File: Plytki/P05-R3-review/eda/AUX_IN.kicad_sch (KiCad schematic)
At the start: 11 parts, among them J6 AUX / coax 50mm, SW1 AUX HI / LO

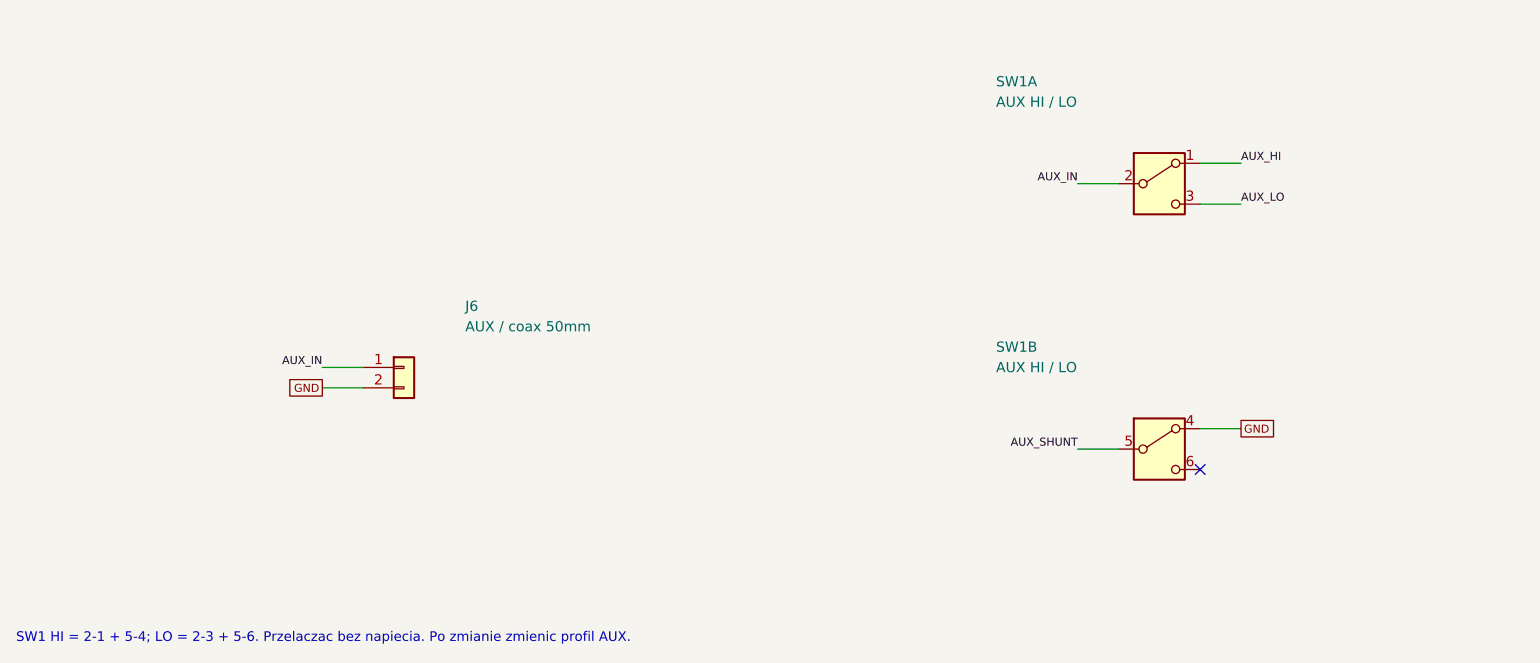
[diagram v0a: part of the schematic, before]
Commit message: P05 R3 (S1) etap 2: typy części — SMD 1206, posiadane THT z rejestru, SW1 JS202011AQN
Rezystory precyzyjne 1206 0,1 %: okno DAQ_OK (R3-R8) 10 ppm/K, dzielniki
kanałów 25 ppm/K. Z rejestru: 47k i 4,7k MF0207 na stojąco, MKT 10n/100n,
MKS2 1u, C0G 1n, logika i 1N4148. Wyjątki: R1 1 W leżący, C1, C12/C13 1210.
SW1: suwak kątowy C&K JS202011AQN (biegun B lustrzany względem 7201).
ERC 0, 464/464 pinów.

Co-Authored-By: Claude Opus 5.5 <noreply@anthropic.com>
Claude-Session: https://claude.ai/code/session_01PNjhiJP63vXoN5NGrWe8up
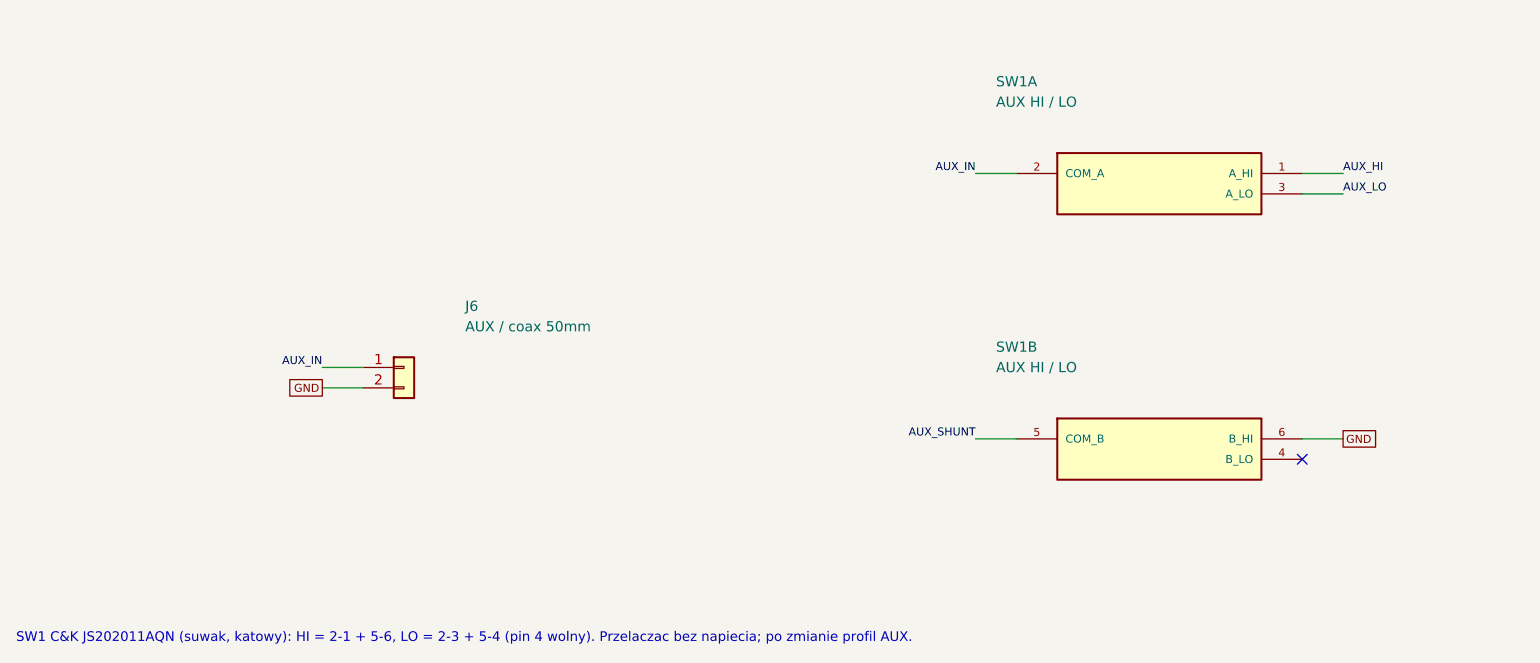
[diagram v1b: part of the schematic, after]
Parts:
- C32: footprint Capacitor_SMD:C_0805_2012Metric -> Capacitor_THT:C_Disc_D5.0mm_W2.5mm_P5.00mm; MPN X7R 25V 10% 1n -> C320C102J1G5TA (KEMET C0G 1n, owned; lead pitch to check on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
- C33, C34: footprint Capacitor_SMD:C_0805_2012Metric -> Capacitor_SMD:C_1206_3216Metric_Pad1.33x1.80mm_HandSolder; MPN C0G 50V 5% 220p -> SMD 1206 C0G 50V 5% 220p
- R30: footprint Resistor_THT:R_Axial_DIN0207_L6.3mm_D2.5mm_P10.16mm_Horizontal -> Resistor_SMD:R_1206_3216Metric_Pad1.30x1.75mm_HandSolder; MPN metal film resistor 10K 1% -> RC1206FR-0710KL
- R31: footprint Resistor_THT:R_Axial_DIN0207_L6.3mm_D2.5mm_P10.16mm_Horizontal -> Resistor_SMD:R_1206_3216Metric_Pad1.30x1.75mm_HandSolder; MPN MBB0207 precision metal film 499K 0.1% -> RT1206BRD07499KL
- R32, R34, R35: footprint Resistor_THT:R_Axial_DIN0207_L6.3mm_D2.5mm_P10.16mm_Horizontal -> Resistor_SMD:R_1206_3216Metric_Pad1.30x1.75mm_HandSolder; MPN MBB0207 precision metal film 100K 0.1% -> RT1206BRD07100KL
- R33: footprint Resistor_THT:R_Axial_DIN0207_L6.3mm_D2.5mm_P10.16mm_Horizontal -> Resistor_SMD:R_1206_3216Metric_Pad1.30x1.75mm_HandSolder; MPN MBB0207 precision metal film 300K 0.1% -> RT1206BRD07300KL
- SW1: footprint P05:CK_7201SYCBE -> Button_Switch_THT:SW_CK_JS202011AQN_DPDT_Angled; symbol P05:CK7201_DPDT -> P05:SW_DPDT_JS202011; MPN 7201SYCBE -> JS202011AQN
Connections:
- net GND: now also SW1.6 (B_HI); no longer SW1.4 (A)
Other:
- note added: "SW1 C&K JS202011AQN (suwak, katowy): HI = 2-1 + 5-6, LO = 2-3 + 5-4 (pin 4 wolny). Przelaczac bez napiecia; po zmianie profil AUX."
- note removed: "SW1 HI = 2-1 + 5-4; LO = 2-3 + 5-6. Przelaczac bez napiecia. Po zmianie zmienic profil AUX."

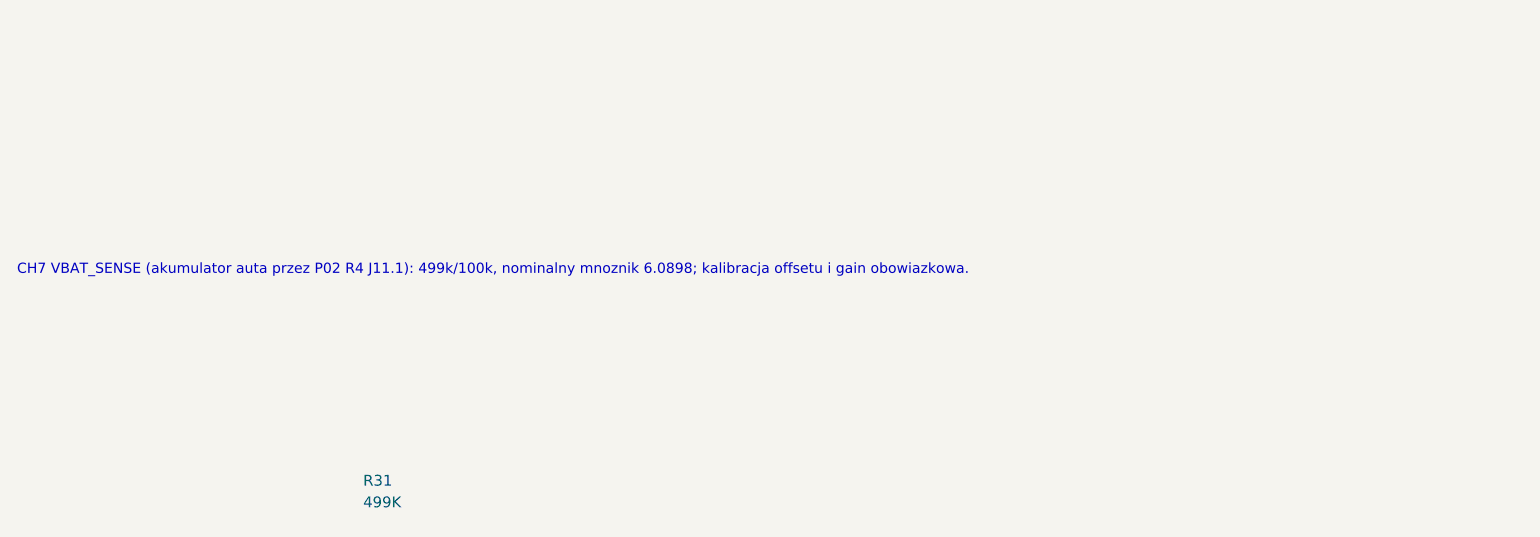
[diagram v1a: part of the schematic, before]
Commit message: P05 R3: poprawki po recenzji lokalnej PR #7 (SW1 czeka na decyzję)
- J_SV1 13 kołków: szyny 5V_SYS/5VA_P05/3V3_DAQ obok siebie i GND, VBAT_SENSE
  między GND (zasada z P03 R6); wewnętrzne GND 3 i 7; R36–R44 bez zmian
- bilans posiadanych części z P02 R4: MKT 10n/100n i WIMA 1µ zostają po 1 szt.,
  więc C2, C23, C16–C18, C25, C26 jako nowe 1206; BOM z kolumną zrodlo
- verify_s1: szyny tylko obok GND / szyn, GND na końcach (wewnątrz dozwolone),
  kolumna rezystorów w SERWIS.csv, nowe mutacje — 26/26, mutacje 33/33
- verify_electrical: budżet dzielników kanałów (0,1 %, 25 ppm/K) w raporcie
- README: punkt otwarty pojemności 5V_SYS (~986 µF wobec 600 µF) i SW1
  (E-Switch pionowy M2 ok. 28 mm wobec 16,5 mm; karta w reference/)
- ODBIOR: kołki J_SV1, pomiar REF_2V5 na C24 albo miernikiem >= 1 GOhm;
  U5B dla DAQ_OK; nieaktualne teksty R2 w PROJEKT, INTEGRACJA, DLA-RECENZENTA

Co-Authored-By: Claude Opus 5.5 <noreply@anthropic.com>
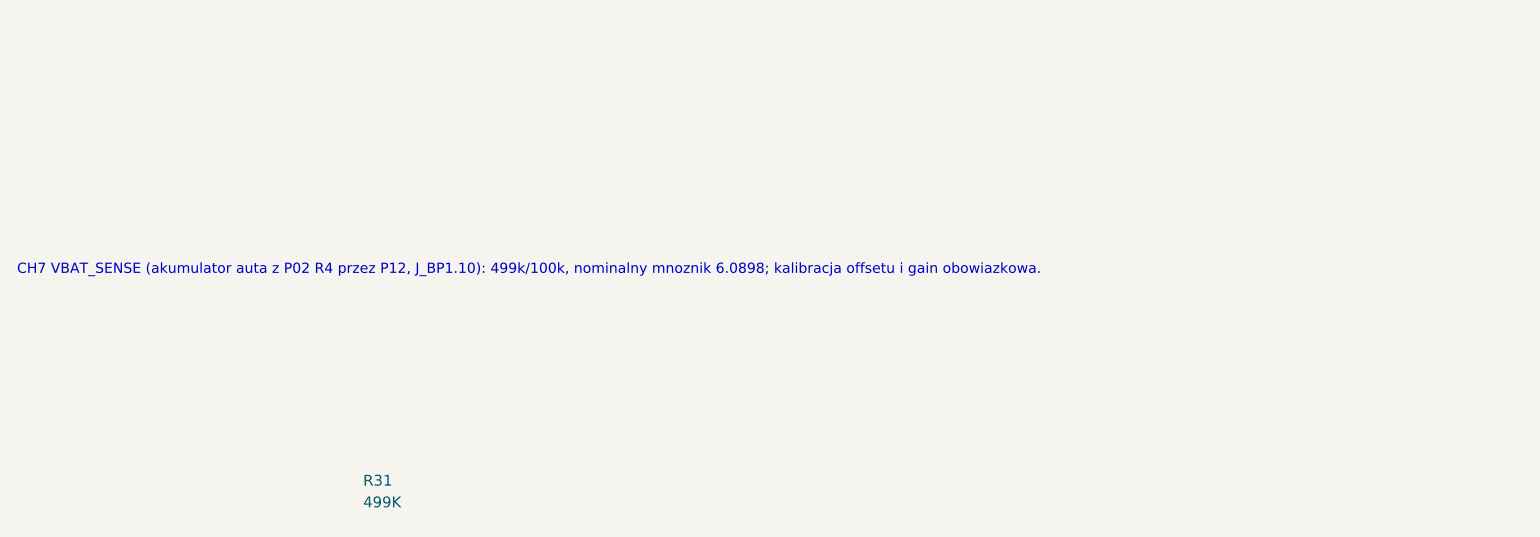
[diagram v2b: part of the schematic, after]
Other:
- note added: "CH7 VBAT_SENSE (akumulator auta z P02 R4 przez P12, J_BP1.10): 499k/100k, nominalny mnoznik 6.0898; kalibracja offsetu i gain obowiazkowa."
- note removed: "CH7 VBAT_SENSE (akumulator auta przez P02 R4 J11.1): 499k/100k, nominalny mnoznik 6.0898; kalibracja offsetu i gain obowiazkowa."

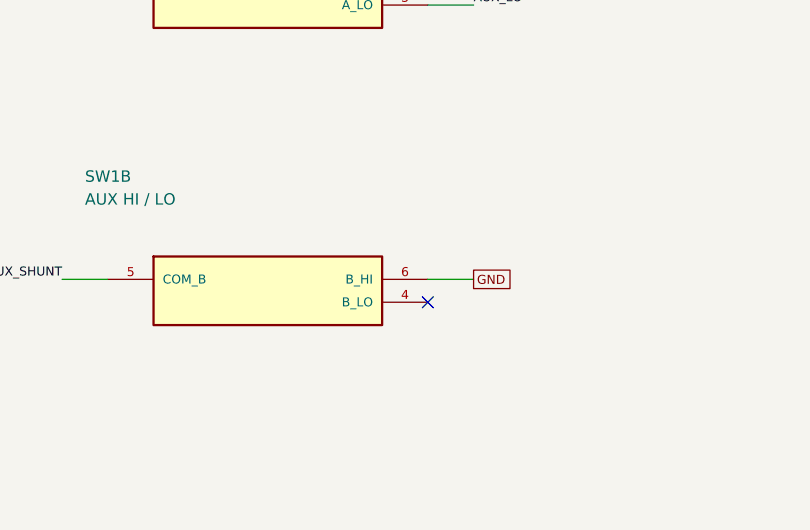
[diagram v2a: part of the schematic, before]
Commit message: P05 R3: SW1 = E-Switch 100 kątowy M6, C1 = 220 µF (decyzje użytkownika 1.10)
- SW1: E-Switch 100 DPDT ON-ON w wersji kątowej M6 zamiast pionowego
  100DP1T1B1M2REH (ok. 28 mm wobec 16,5 mm); footprint P05:ESW_100DP_M6 z rysunku
  M6-DP (karta s. 11); styki jak w R2 (HI 2-1 + 5-4), więc obwód R2 bez wyjątków
- C1 220 µF (EEUFR1C221, D6,3): z P06 C3 220 µF razem ok. 486 µF na 5 V
- kontrola SW1 z geometrii dla biegunów w kolumnach; mutacje bez zmian liczby
- kontrole: ERC 0, 466/466 pinów, elektryczne 21/21 (12/12), S1 26/26 (33/33)

Co-Authored-By: Claude Opus 5.5 <noreply@anthropic.com>
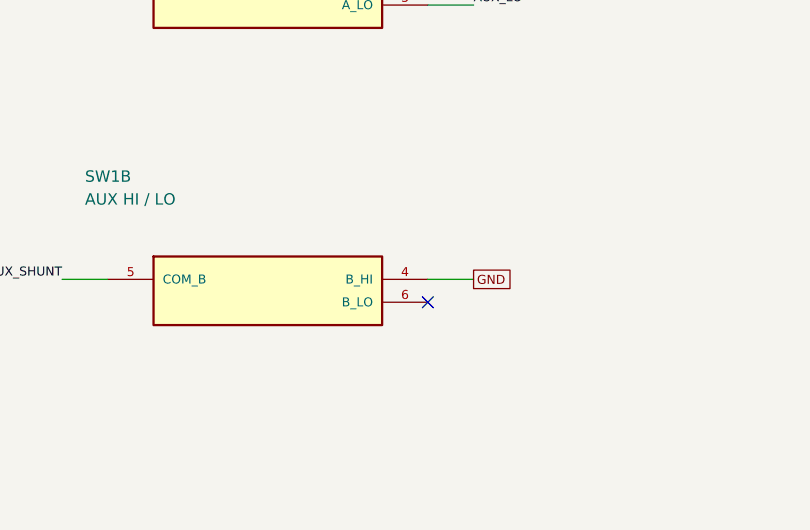
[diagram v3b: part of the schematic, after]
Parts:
- SW1: footprint Button_Switch_THT:SW_CK_JS202011AQN_DPDT_Angled -> P05:ESW_100DP_M6; symbol P05:SW_DPDT_JS202011 -> P05:SW_DPDT_ESW100; MPN JS202011AQN -> 100DP1T1B4M6RE (E-Switch 100, DPDT ON-ON, M6 right angle, g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
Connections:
- net GND: now also SW1.4 (B_HI); no longer SW1.6 (B_HI)
